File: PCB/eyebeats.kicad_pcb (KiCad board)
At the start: 2 copper layers, 97.5 x 56.5 mm, 47 parts, among them SW1 1825910-6, SW2 1825910-6, U1 MAX30102EFD_T, U2 XIAO-RP2040-DIP, U3 PCF8574T, U4 AMS1117-1.8

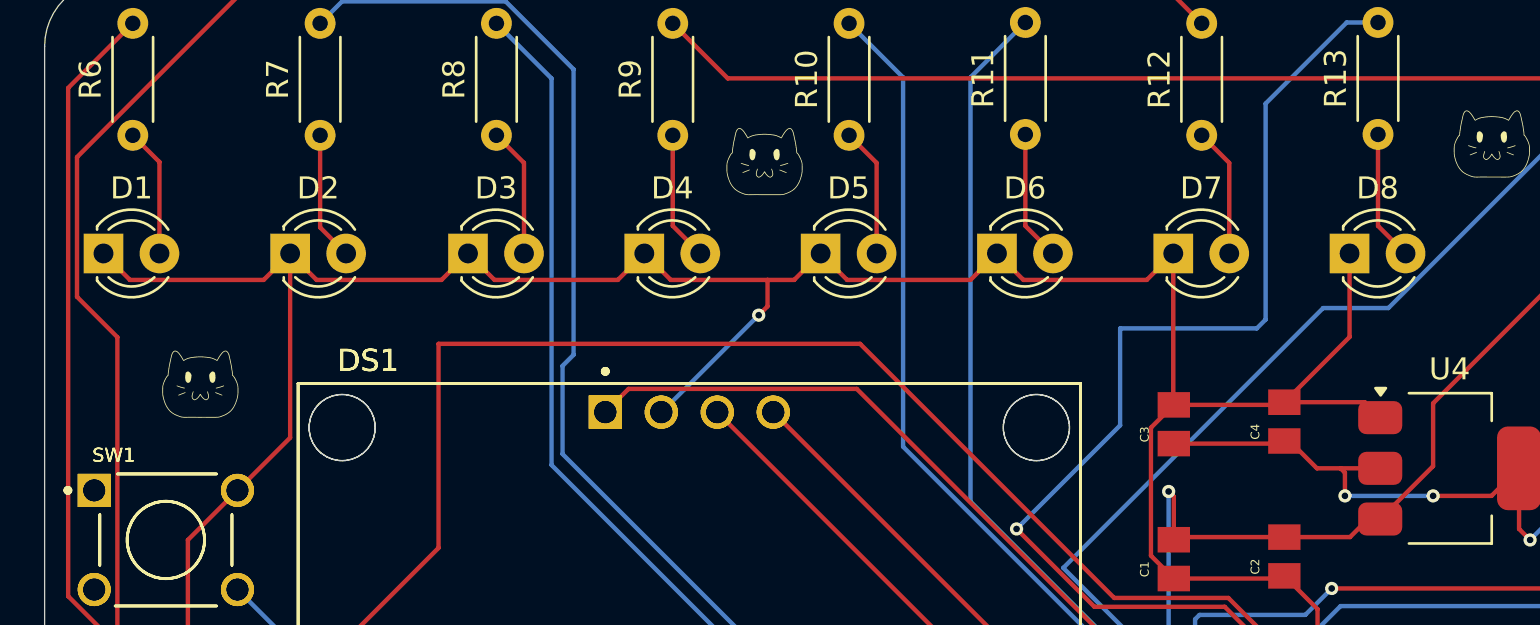
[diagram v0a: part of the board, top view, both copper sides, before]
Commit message: edited led directions in pcb and more codeee
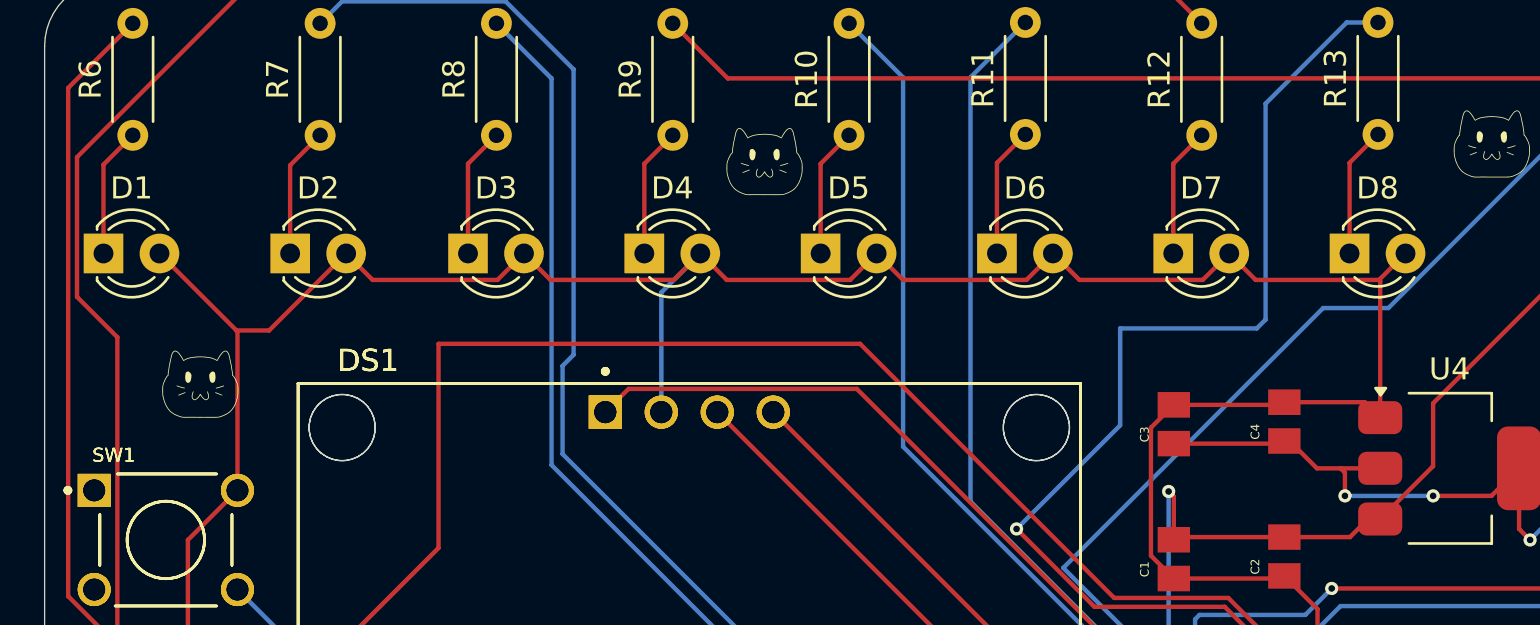
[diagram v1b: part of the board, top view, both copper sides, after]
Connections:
- D1 pad 1: GND -> Net-(D1-K)
- D1 pad 2: Net-(D1-A) -> GND
- D2 pad 1: GND -> Net-(D2-K)
- D2 pad 2: Net-(D2-A) -> GND
- D3 pad 1: GND -> Net-(D3-K)
- D3 pad 2: Net-(D3-A) -> GND
- D4 pad 1: GND -> Net-(D4-K)
- D4 pad 2: Net-(D4-A) -> GND
- D5 pad 1: GND -> Net-(D5-K)
- D5 pad 2: Net-(D5-A) -> GND
- D6 pad 1: GND -> Net-(D6-K)
- D6 pad 2: Net-(D6-A) -> GND
- D7 pad 1: GND -> Net-(D7-K)
- D7 pad 2: Net-(D7-A) -> GND
- D8 pad 1: GND -> Net-(D8-K)
- D8 pad 2: Net-(D8-A) -> GND
- R10 pad 1: Net-(D5-A) -> Net-(D5-K)
- R11 pad 1: Net-(D6-A) -> Net-(D6-K)
- R12 pad 1: Net-(D7-A) -> Net-(D7-K)
- R13 pad 1: Net-(D8-A) -> Net-(D8-K)
- R6 pad 1: Net-(D1-A) -> Net-(D1-K)
- R7 pad 1: Net-(D2-A) -> Net-(D2-K)
- R8 pad 1: Net-(D3-A) -> Net-(D3-K)
- R9 pad 1: Net-(D4-A) -> Net-(D4-K)
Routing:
- net Net-(D8-K): track 0.00 -> 5.93 mm
- net Net-(D6-K): track 0.00 -> 5.93 mm
- net Net-(D2-K): track 0.00 -> 5.92 mm
- net Net-(D8-A): track 5.92 -> 0.00 mm
- net Net-(D6-A): track 5.92 -> 0.00 mm
- net Net-(D1-K): track 0.00 -> 5.91 mm
- net Net-(D4-K): track 0.00 -> 5.89 mm
- net Net-(D3-K): track 0.00 -> 5.89 mm
- net Net-(D7-K): track 0.00 -> 5.89 mm
- net Net-(D5-K): track 0.00 -> 5.89 mm
- net Net-(D7-A): track 5.88 -> 0.00 mm
- net Net-(D5-A): track 5.88 -> 0.00 mm
- net Net-(D4-A): track 5.88 -> 0.00 mm
- net Net-(D3-A): track 5.88 -> 0.00 mm
- net Net-(D1-A): track 5.86 -> 0.00 mm
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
